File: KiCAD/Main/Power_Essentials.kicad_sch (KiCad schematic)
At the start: 26 parts, among them J1 Micro_SD_Card_Det2, J2 Screw_Terminal_01x09, J3 Screw_Terminal_01x09, J4 USB_C_Receptacle_USB2.0_16P, Q1 AO3400A, Q2 AO3400A, Q3 AO3400A, U1 LM2596S-3.3, U2 TPS2121RUXR

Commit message: Fixed footprints for terminal blocks
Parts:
- J2, J3: footprint Connector_Phoenix_MSTB:PhoenixContact_MSTBVA_2,5_9-G_1x09_P5.00mm_Vertical -> TerminalBlock_Phoenix:TerminalBlock_Phoenix_MKDS-1,5-9_1x09_P5.00mm_Horizontal
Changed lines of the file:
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@@
 			)
 		)
-		(property "Footprint" "Connector_Phoenix_MSTB:PhoenixContact_MSTBVA_2,5_9-G_1x09_P5.00mm_Vertical"
+		(property "Footprint" "TerminalBlock_Phoenix:TerminalBlock_Phoenix_MKDS-1,5-9_1x09_P5.00mm_Horizontal"
 			(at 238.76 133.35 0)
 			(effects
@@
 			)
 		)
-		(property "Footprint" "Connector_Phoenix_MSTB:PhoenixContact_MSTBVA_2,5_9-G_1x09_P5.00mm_Vertical"
+		(property "Footprint" "TerminalBlock_Phoenix:TerminalBlock_Phoenix_MKDS-1,5-9_1x09_P5.00mm_Horizontal"
 			(at 214.63 133.35 0)
 			(effects

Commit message: Layout and routing
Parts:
- D2: now not fitted
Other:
- note added: "D2 is marked as DNF, since it is placed on the back and will be hand soldered instead of assembled"
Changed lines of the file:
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@@
 	(generator_version "9.0")
 	(paper "A4")
+	(text "D2 is marked as DNF, \nsince it is placed on \nthe back and will be \nhand soldered instead \nof assembled"
+		(exclude_from_sim no)
+		(at 151.384 140.208 0)
+		(effects
+			(font
+				(size 1.27 1.27)
+			)
+		)
+	)
 	(junction
 		(at 215.9 72.39)
@@
 		(in_bom yes)
 		(on_board yes)
-		(dnp no)
+		(dnp yes)
 		(fields_autoplaced yes)
 		(property "Reference" "D2"

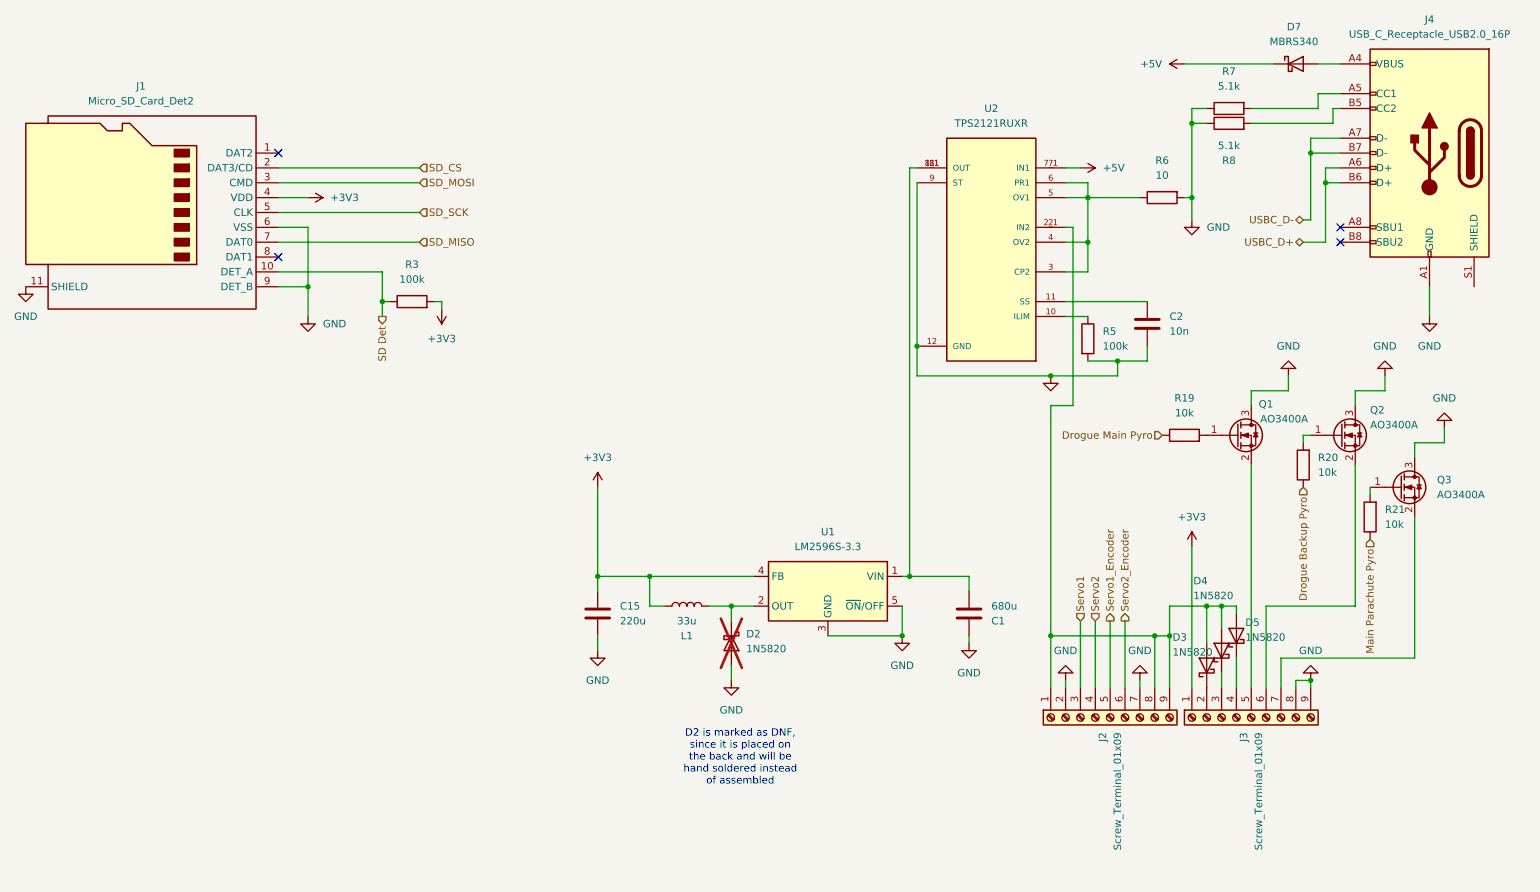
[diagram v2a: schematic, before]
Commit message: Update aux magnetometer, test THs, and silkscreens
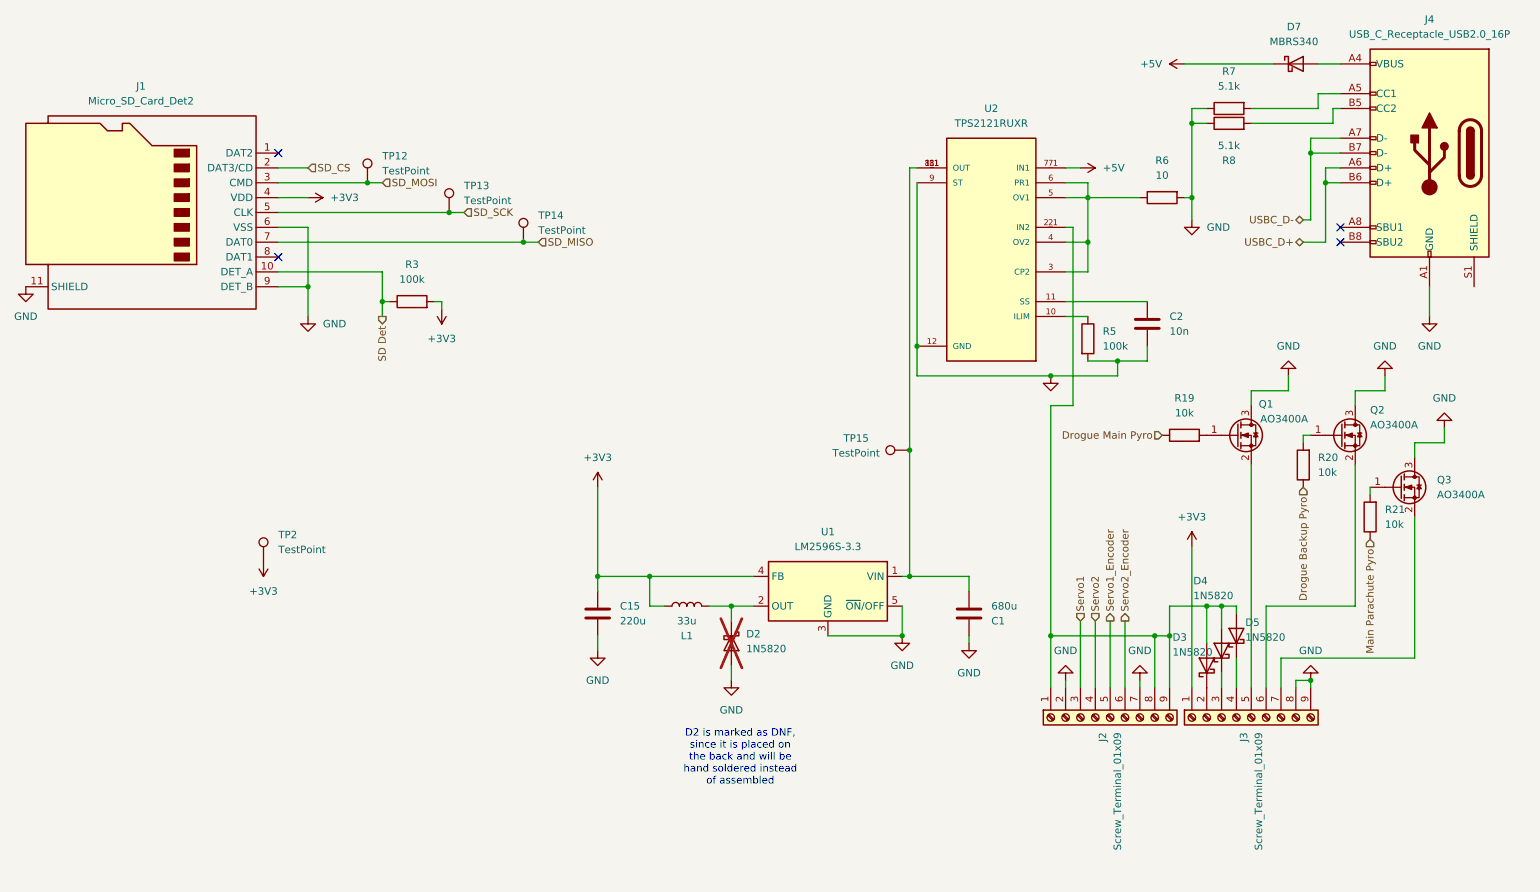
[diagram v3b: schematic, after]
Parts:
- added TP12, TP13, TP14, TP15, TP2: TestPoint, TestPoint:TestPoint_THTPad_1.5x1.5mm_Drill0.7mm, symbol Connector:TestPoint
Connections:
- net +3V3: now also TP2.1
- net SD_MISO: now also TP14.1
- net SD_MOSI: now also TP12.1
- net SD_SCK: now also TP13.1
- net at C1.2, U1.1 (VIN), U2.1 (OUT)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: now also TP15.1

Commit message: Replace independent magnetometer, reformat test points, generate test gerber and BOM
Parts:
- TP12, TP13, TP14, TP15, TP2: footprint TestPoint:TestPoint_THTPad_1.5x1.5mm_Drill0.7mm -> TestPoint:TestPoint_Pad_D1.0mm
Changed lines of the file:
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@@
 			)
 		)
-		(property "Footprint" "TestPoint:TestPoint_THTPad_1.5x1.5mm_Drill0.7mm"
+		(property "Footprint" "TestPoint:TestPoint_Pad_D1.0mm"
 			(at 92.71 41.91 0)
 			(effects
@@
 			)
 		)
-		(property "Footprint" "TestPoint:TestPoint_THTPad_1.5x1.5mm_Drill0.7mm"
+		(property "Footprint" "TestPoint:TestPoint_Pad_D1.0mm"
 			(at 106.68 46.99 0)
 			(effects
@@
 			)
 		)
-		(property "Footprint" "TestPoint:TestPoint_THTPad_1.5x1.5mm_Drill0.7mm"
+		(property "Footprint" "TestPoint:TestPoint_Pad_D1.0mm"
 			(at 180.34 82.55 0)
 			(effects
@@
 			)
 		)
-		(property "Footprint" "TestPoint:TestPoint_THTPad_1.5x1.5mm_Drill0.7mm"
+		(property "Footprint" "TestPoint:TestPoint_Pad_D1.0mm"
 			(at 74.93 106.68 0)
 			(effects
@@
 			)
 		)
-		(property "Footprint" "TestPoint:TestPoint_THTPad_1.5x1.5mm_Drill0.7mm"
+		(property "Footprint" "TestPoint:TestPoint_Pad_D1.0mm"
 			(at 119.38 52.07 0)
 			(effects

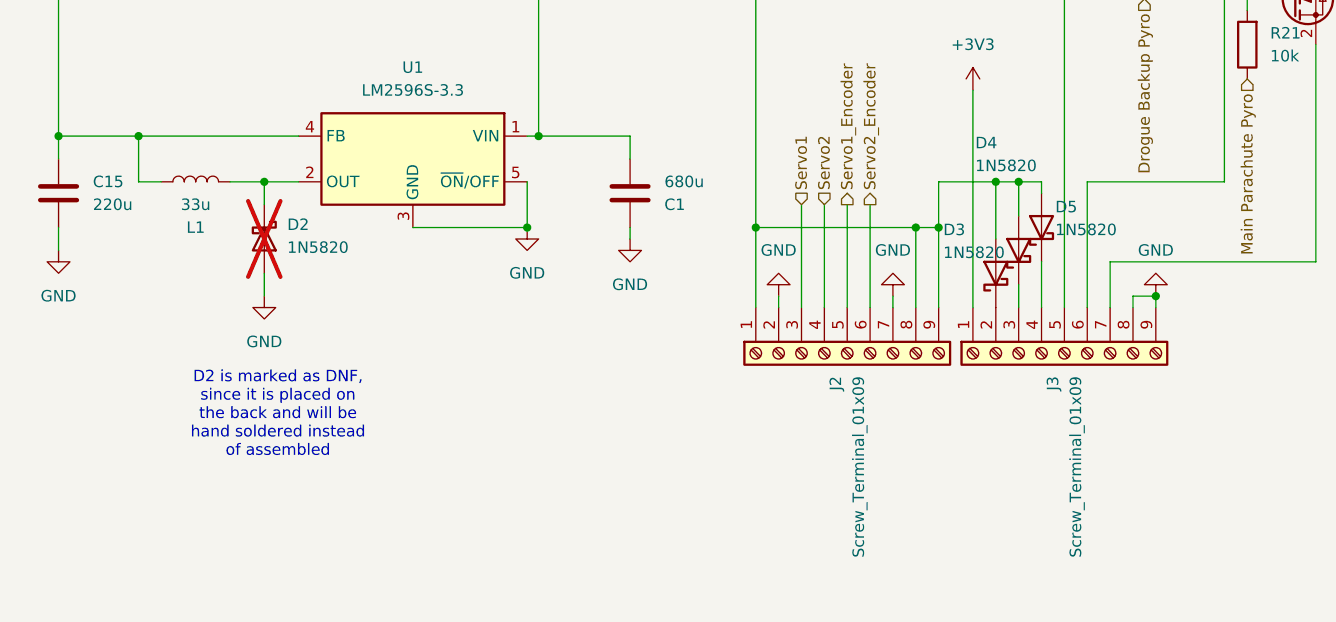
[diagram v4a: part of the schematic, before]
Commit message: Update BOM and respective components according to LCSC supply, remove previously generated production files
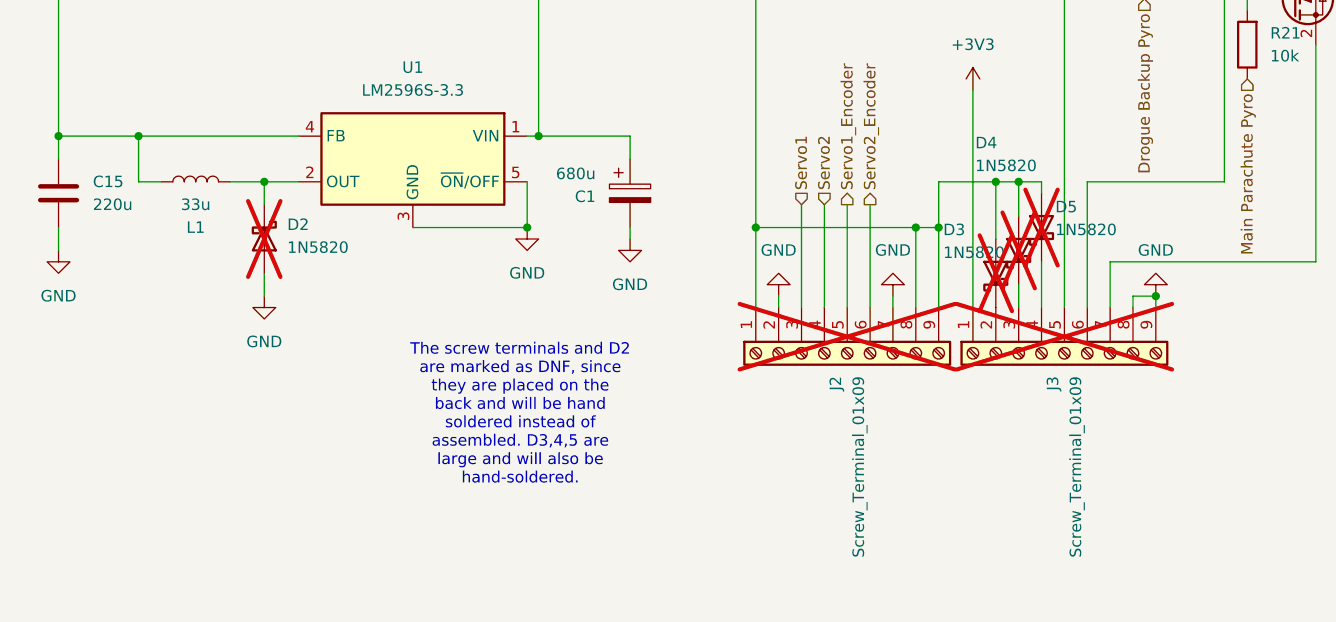
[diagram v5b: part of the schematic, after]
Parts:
- C1: footprint Capacitor_SMD:C_0603_1608Metric -> Capacitor_SMD:CP_Elec_10x12.6; symbol Device:C -> Device:C_Polarized
- C15: footprint Capacitor_SMD:C_0603_1608Metric -> Capacitor_SMD:C_1206_3216Metric
- D2, TP12, TP13, TP14, TP15, TP2: now left out of the parts list
- D3, D4, D5, J2, J3: now not fitted; now left out of the parts list
- L1: footprint Inductor_SMD:L_0603_1608Metric -> Inductor_SMD:L_SXN_SMDRI127
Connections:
- net GND: now also C1.2; no longer C1.1
- net at TP15.1, U1.1 (VIN), U2.1 (OUT)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: now also C1.1; no longer C1.2
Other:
- note added: "The screw terminals and D2 are marked as DNF, since they are placed on the back and will be hand soldered instead of assembled. D3,4,5 are large and will also be hand-soldered."
- note removed: "D2 is marked as DNF, since it is placed on the back and will be hand soldered instead of assembled"
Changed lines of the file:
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@@
 	(generator_version "9.0")
 	(paper "A4")
-	(text "D2 is marked as DNF, \nsince it is placed on \nthe back and will be \nhand soldered instead \nof assembled"
+	(text "The screw terminals and D2 \nare marked as DNF, since \nthey are placed on the \nback and will be hand \nsoldered instead of \nassembled. D3,4,5 are \nlarge and will also be\nhand-soldered."
 		(exclude_from_sim no)
-		(at 151.384 140.208 0)
+		(at 178.308 140.208 0)
 		(effects
 			(font
@@
 			)
 		)
-		(property "Footprint" "Capacitor_SMD:C_0603_1608Metric"
+		(property "Footprint" "Capacitor_SMD:C_1206_3216Metric"
 			(at 127.9652 119.38 0)
 			(effects
@@
 			)
 		)
-		(property "Footprint" "Inductor_SMD:L_0603_1608Metric"
+		(property "Footprint" "Inductor_SMD:L_SXN_SMDRI127"
 			(at 142.24 114.3 0)
 			(effects
@@
 		(unit 1)
 		(exclude_from_sim no)
-		(in_bom yes)
+		(in_bom no)
 		(on_board yes)
 		(dnp no)
@@
 	)
 	(symbol
-		(lib_id "Device:C")
+		(lib_id "Device:C_Polarized")
 		(at 190.5 115.57 0)
-		(mirror x)
 		(unit 1)
 		(exclude_from_sim no)
@@
 		(on_board yes)
 		(dnp no)
-		(fields_autoplaced yes)
 		(property "Reference" "C1"
-			(at 194.31 116.84 0)
+			(at 186.69 115.9511 0)
 			(effects
 				(font
 					(size 1.27 1.27)
 				)
-				(justify left)
+				(justify right)
 			)
 		)
 		(property "Value" "680u"
-			(at 194.31 114.3 0)
+			(at 186.69 113.4111 0)
 			(effects
 				(font
 					(size 1.27 1.27)
 				)
-				(justify left)
+				(justify right)
 			)
 		)
-		(property "Footprint" "Capacitor_SMD:C_0603_1608Metric"
-			(at 191.4652 111.76 0)
+		(property "Footprint" "Capacitor_SMD:CP_Elec_10x12.6"
+			(at 191.4652 119.38 0)
 			(effects
 				(font
@@
 			)
 		)
-		(property "Description" "Unpolarized capacitor"
+		(property "Description" "Polarized capacitor"
 			(at 190.5 115.57 0)
 			(effects
@@
 		(unit 1)
 		(exclude_from_sim no)
-		(in_bom yes)
+		(in_bom no)
 		(on_board yes)
 		(dnp no)
@@
 		(unit 1)
 		(exclude_from_sim no)
-		(in_bom yes)
+		(in_bom no)
 		(on_board yes)
 		(dnp yes)
@@
 		(unit 1)
 		(exclude_from_sim no)
-		(in_bom yes)
+		(in_bom no)
 		(on_board yes)
-		(dnp no)
+		(dnp yes)
 		(property "Reference" "D3"
 			(at 225.298 119.634 90)
@@
 		(unit 1)
 		(exclude_from_sim no)
-		(in_bom yes)
+		(in_bom no)
 		(on_board yes)
-		(dnp no)
+		(dnp yes)
 		(property "Reference" "D5"
 			(at 237.744 117.094 90)
@@
 		(unit 1)
 		(exclude_from_sim no)
-		(in_bom yes)
+		(in_bom no)
 		(on_board yes)
 		(dnp no)
@@
 		(unit 1)
 		(exclude_from_sim no)
-		(in_bom yes)
+		(in_bom no)
 		(on_board yes)
 		(dnp no)
@@
 		(unit 1)
 		(exclude_from_sim no)
-		(in_bom yes)
+		(in_bom no)
 		(on_board yes)
-		(dnp no)
+		(dnp yes)
 		(property "Reference" "D4"
 			(at 228.854 109.982 90)
@@
 		(unit 1)
 		(exclude_from_sim no)
-		(in_bom yes)
+		(in_bom no)
 		(on_board yes)
-		(dnp no)
+		(dnp yes)
 		(fields_autoplaced yes)
 		(property "Reference" "J3"
@@
 		(unit 1)
 		(exclude_from_sim no)
-		(in_bom yes)
+		(in_bom no)
 		(on_board yes)
 		(dnp no)
@@
 		(unit 1)
 		(exclude_from_sim no)
-		(in_bom yes)
+		(in_bom no)
 		(on_board yes)
-		(dnp no)
+		(dnp yes)
 		(fields_autoplaced yes)
 		(property "Reference" "J2"

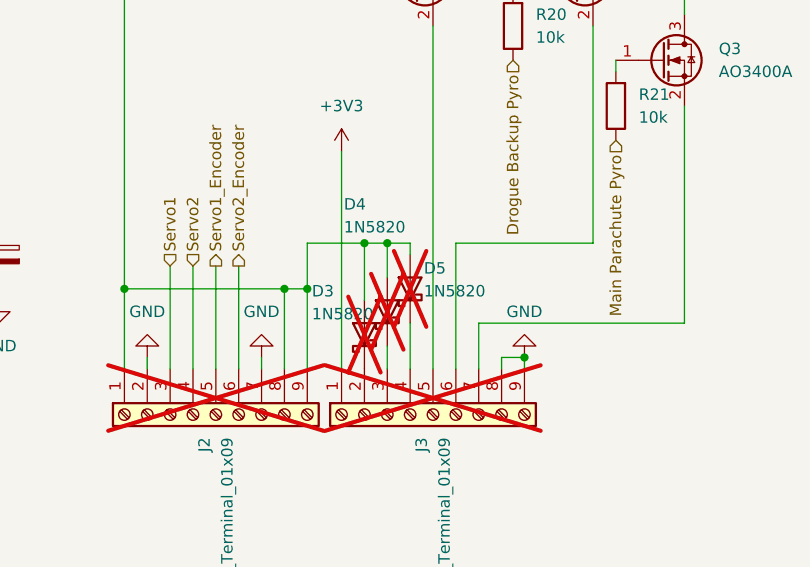
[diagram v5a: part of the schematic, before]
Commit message: save after realizing branch was not switched to layoutv2
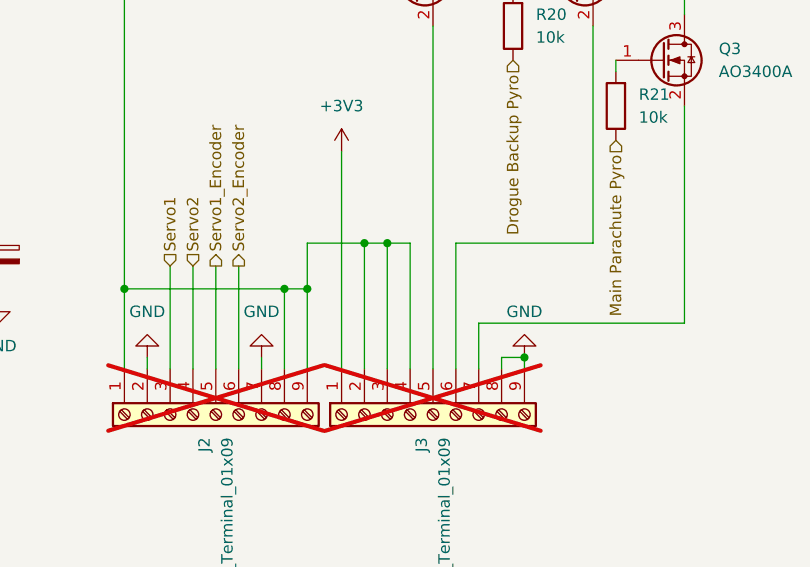
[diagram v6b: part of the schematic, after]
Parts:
- removed D3, D4, D5: 1N5820, Diode_THT:D_DO-201AD_P15.24mm_Horizontal, symbol Diode:1N5820
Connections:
- net at J2.1 (7.4V_IN), J2.8 (MotorPwr1), J2.9 (MotorPwr2)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: now also J3.2 (Pyro_OUT_1), J3.3 (Pyro_OUT_2), J3.4 (Pyro_OUT_3)
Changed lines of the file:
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@@
 	(wire
 		(pts
-			(xy 236.22 123.19) (xy 236.22 128.27)
+			(xy 236.22 114.3) (xy 236.22 128.27)
 		)
 		(stroke
@@
 	(wire
 		(pts
-			(xy 231.14 114.3) (xy 231.14 120.65)
+			(xy 231.14 114.3) (xy 231.14 128.27)
 		)
 		(stroke
@@
 	(wire
 		(pts
-			(xy 233.68 114.3) (xy 233.68 118.11)
-		)
-		(stroke
-			(width 0)
-			(type default)
-		)
-	)
-	(wire
-		(pts
-			(xy 233.68 125.73) (xy 233.68 128.27)
+			(xy 233.68 114.3) (xy 233.68 128.27)
 		)
 		(stroke
@@
 	(wire
 		(pts
-			(xy 236.22 114.3) (xy 236.22 115.57)
-		)
-		(stroke
-			(width 0)
-			(type default)
-		)
-	)
-	(wire
-		(pts
 			(xy 248.92 127) (xy 248.92 128.27)
 		)
@@
 	)
 	(symbol
-		(lib_id "Diode:1N5820")
-		(at 231.14 124.46 90)
-		(unit 1)
-		(exclude_from_sim no)
-		(in_bom no)
-		(on_board yes)
-		(dnp yes)
-		(property "Reference" "D3"
-			(at 225.298 119.634 90)
-			(effects
-				(font
-					(size 1.27 1.27)
-				)
-				(justify right)
-			)
-		)
-		(property "Value" "1N5820"
-			(at 225.298 122.174 90)
-			(effects
-				(font
-					(size 1.27 1.27)
-				)
-				(justify right)
-			)
-		)
-		(property "Footprint" "Diode_THT:D_DO-201AD_P15.24mm_Horizontal"
-			(at 235.585 124.46 0)
-			(effects
-				(font
-					(size 1.27 1.27)
-				)
-				(hide yes)
-			)
-		)
-		(property "Datasheet" "http://www.vishay.com/docs/88526/1n5820.pdf"
-			(at 231.14 124.46 0)
-			(effects
-				(font
-					(size 1.27 1.27)
-				)
-				(hide yes)
-			)
-		)
-		(property "Description" "20V 3A Schottky Barrier Rectifier Diode, DO-201AD"
-			(at 231.14 124.46 0)
-			(effects
-				(font
-					(size 1.27 1.27)
-				)
-				(hide yes)
-			)
-		)
-		(pin "1"
-		)
-		(pin "2"
-		)
-		(instances
-			(project ""
-				(path "/bbb10697-a5dd-43b8-9c6f-4c5919cf3463/14279dde-67ce-4c97-8b3d-bab2d340dd8b"
-					(reference "D3")
-					(unit 1)
-				)
-			)
-		)
-	)
-	(symbol
 		(lib_id "Regulator_Switching:LM2596S-3.3")
 		(at 166.37 111.76 0)
@@
 	)
 	(symbol
-		(lib_id "Diode:1N5820")
-		(at 236.22 119.38 90)
-		(unit 1)
-		(exclude_from_sim no)
-		(in_bom no)
-		(on_board yes)
-		(dnp yes)
-		(property "Reference" "D5"
-			(at 237.744 117.094 90)
-			(effects
-				(font
-					(size 1.27 1.27)
-				)
-				(justify right)
-			)
-		)
-		(property "Value" "1N5820"
-			(at 237.744 119.634 90)
-			(effects
-				(font
-					(size 1.27 1.27)
-				)
-				(justify right)
-			)
-		)
-		(property "Footprint" "Diode_THT:D_DO-201AD_P15.24mm_Horizontal"
-			(at 240.665 119.38 0)
-			(effects
-				(font
-					(size 1.27 1.27)
-				)
-				(hide yes)
-			)
-		)
-		(property "Datasheet" "http://www.vishay.com/docs/88526/1n5820.pdf"
-			(at 236.22 119.38 0)
-			(effects
-				(font
-					(size 1.27 1.27)
-				)
-				(hide yes)
-			)
-		)
-		(property "Description" "20V 3A Schottky Barrier Rectifier Diode, DO-201AD"
-			(at 236.22 119.38 0)
-			(effects
-				(font
-					(size 1.27 1.27)
-				)
-				(hide yes)
-			)
-		)
-		(pin "1"
-		)
-		(pin "2"
-		)
-		(instances
-			(project "Main"
-				(path "/bbb10697-a5dd-43b8-9c6f-4c5919cf3463/14279dde-67ce-4c97-8b3d-bab2d340dd8b"
-					(reference "D5")
-					(unit 1)
-				)
-			)
-		)
-	)
-	(symbol
 		(lib_id "power:GND")
 		(at 149.86 127 0)
@@
 					(unit 1)
 				)
-			)
-		)
-	)
-	(symbol
-		(lib_id "Diode:1N5820")
-		(at 233.68 121.92 90)
-		(unit 1)
-		(exclude_from_sim no)
-		(in_bom no)
-		(on_board yes)
-		(dnp yes)
-		(property "Reference" "D4"
-			(at 228.854 109.982 90)
-			(effects
-				(font
-					(size 1.27 1.27)
-				)
-				(justify right)
-			)
-		)
-		(property "Value" "1N5820"
-			(at 228.854 112.522 90)
-			(effects
-				(font
-					(size 1.27 1.27)
-				)
-				(justify right)
-			)
-		)
-		(property "Footprint" "Diode_THT:D_DO-201AD_P15.24mm_Horizontal"
-			(at 238.125 121.92 0)
-			(effects
-				(font
-					(size 1.27 1.27)
-				)
-				(hide yes)
-			)
-		)
-		(property "Datasheet" "http://www.vishay.com/docs/88526/1n5820.pdf"
-			(at 233.68 121.92 0)
-			(effects
-				(font
-					(size 1.27 1.27)
-				)
-				(hide yes)
-			)
-		)
-		(property "Description" "20V 3A Schottky Barrier Rectifier Diode, DO-201AD"
-			(at 233.68 121.92 0)
-			(effects
-				(font
-					(size 1.27 1.27)
-				)
-				(hide yes)
-			)
-		)
-		(pin "1"
-		)
-		(pin "2"
-		)
-		(instances
-			(project "Main"
-				(path "/bbb10697-a5dd-43b8-9c6f-4c5919cf3463/14279dde-67ce-4c97-8b3d-bab2d340dd8b"
-					(reference "D4")
-					(unit 1)
-				)
